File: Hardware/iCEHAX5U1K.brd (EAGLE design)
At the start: 60.9 x 17.8 mm, 28 parts, among them IC1 ICE5LP1K-SG48, IC2 XC6206P331MR-G, IC3 XC6206P122MR-G, IC4 STM32F042F6P6, IC5 BR24G1MFJ-3AGTE2

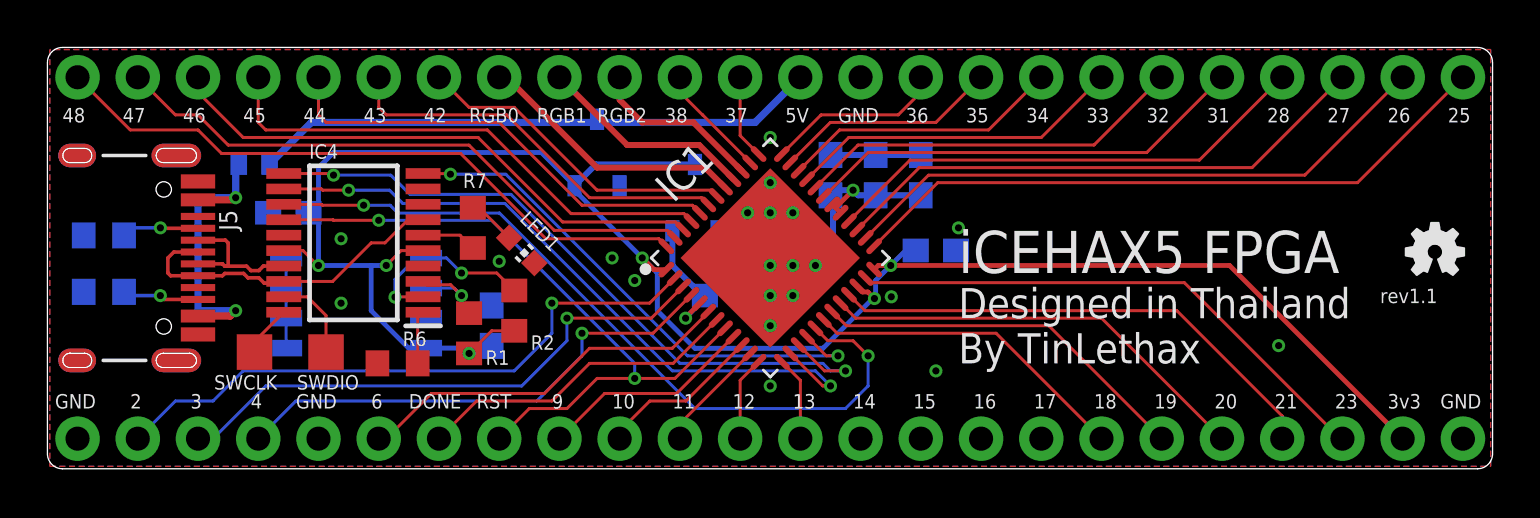
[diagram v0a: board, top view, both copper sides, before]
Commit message: Top PIO Bank design issue fixed. - Top PIO Bank (Pin 25 and up) was missing the VCC_IO rail due to confusion of pin 33.
Signed-off-by: Tin LetHax <thipok17@gmail.com>
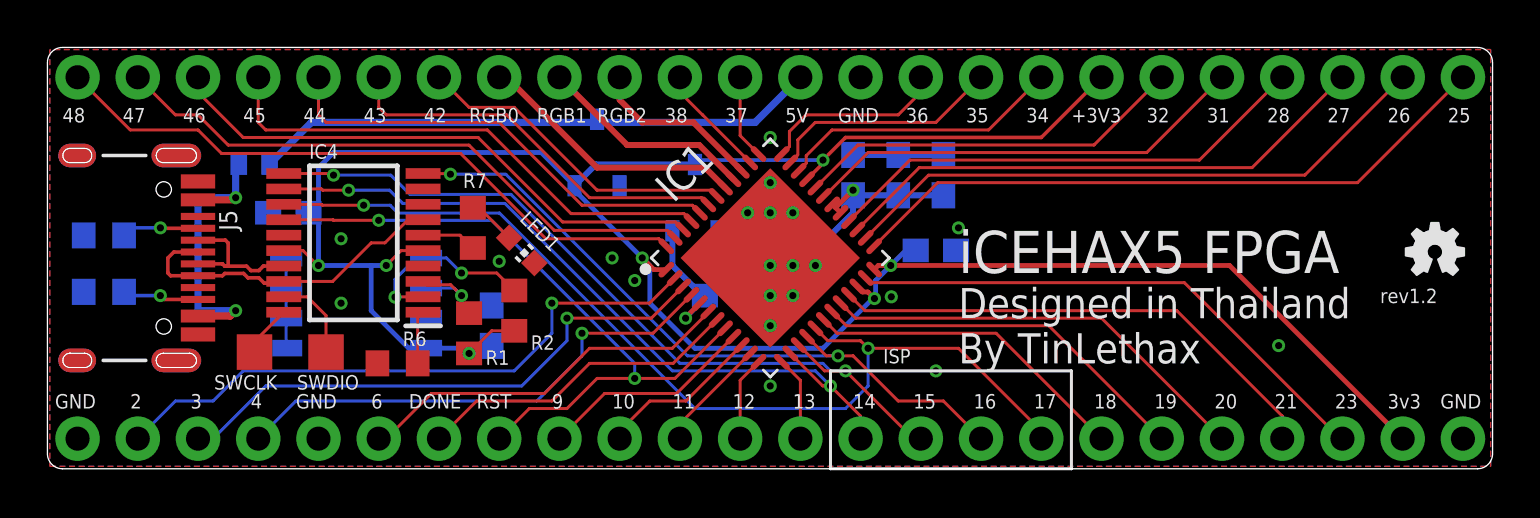
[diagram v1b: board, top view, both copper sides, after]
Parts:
- moved C5 0.95 mm to (35.9, 12.4)
- moved C6 0.95 mm to (37.8, 12.4)
- moved C4 0.95 mm to (34.0, 12.4)
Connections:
- removed net IO14: J2.2
- removed net IO15: J2.3
- removed net IO16: J2.4
- removed net IO17: J2.5
- removed net IO33: IC1.33, J3.6
- net +3V3: now also IC1.33, J3.6
- net SCK: now also J2.3
- net SI: now also J2.5
- net SO: now also J2.2
- net SS: now also J2.4
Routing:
- net +3V3: track 89.2 -> 109.0 mm, vias 6 -> 7
- net IO33: track 14.2 -> 0.00 mm
- net SI: track 32.6 -> 41.8 mm
- net SS: track 22.3 -> 29.8 mm
- net SCK: track 29.6 -> 33.9 mm
- net SO: track 28.8 -> 31.5 mm
- net +1V2: track 19.3 -> 19.9 mm
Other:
- board text added: "+3V3"
- board text added: "ISP"
- board text added: "rev1.2"
- board text removed: "33"
- board text removed: "rev1.1"
